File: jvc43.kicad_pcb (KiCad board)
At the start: 6 copper layers, 101.6 x 50.8 mm, 137 parts, among them J201 8P8C_LED_Shielded, J301 8P8C_LED_Shielded, J401 USB_C_Receptacle_USB2.0, U201 LAN8810, U301 LAN8810, U401 LTC3622*DE, X101 25 MHz

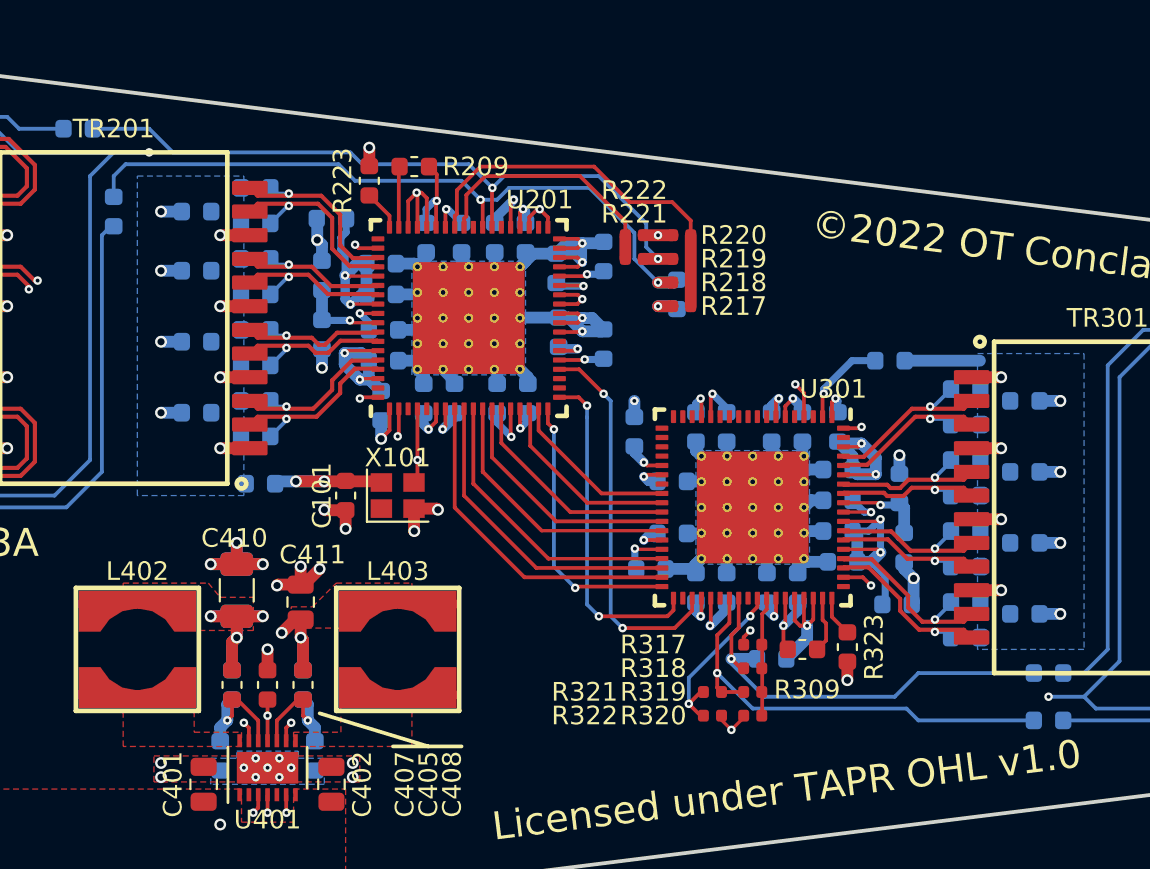
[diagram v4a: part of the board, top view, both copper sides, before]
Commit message: Added RC+D circuits for power-on reset of PHY chips.  Running out of room...
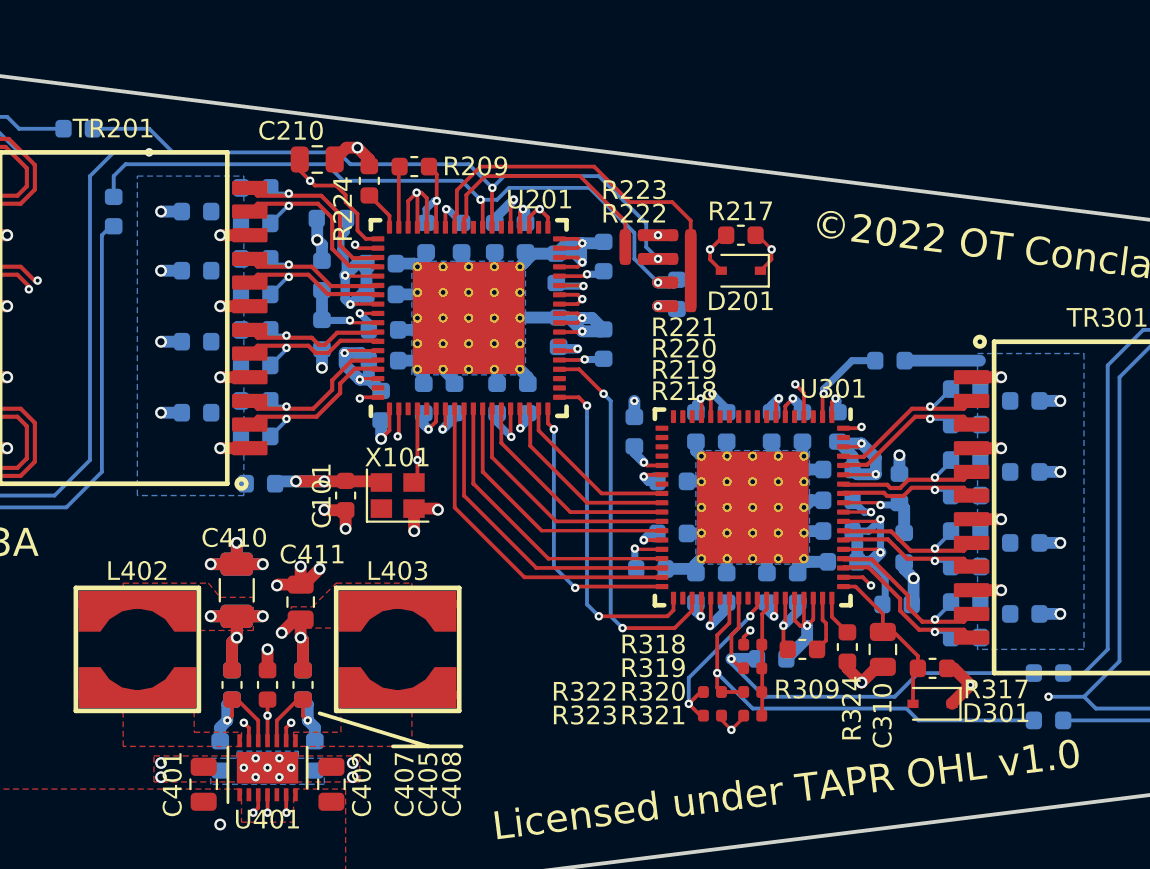
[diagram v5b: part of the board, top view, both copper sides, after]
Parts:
- added C210: 10u, Capacitor_SMD:C_0805_2012Metric, F.Cu at (60.5, 32.1)
- added C310: 10u, Capacitor_SMD:C_0805_2012Metric, F.Cu at (90.8, 58.4)
- added D201: 1N4148WS, Diode_SMD:D_SOD-323, F.Cu at (83.2, 38.1)
- added D301: 1N4148WS, Diode_SMD:D_SOD-323, F.Cu at (93.5, 61.3)
- added R217: 5k1, Resistor_SMD:R_0603_1608Metric, F.Cu at (83.2, 36.2)
- added R317: 5k1, Resistor_SMD:R_0603_1608Metric, F.Cu at (93.5, 59.4)
- renumbered C210 to C211, C211 to C212, C212 to C213, C213 to C214, C214 to C215, C215 to C216, C216 to C217, C217 to C218, C218 to C219, C219 to C220, C220 to C221, C221 to C222, C222 to C223, C223 to C224, C224 to C225, C225 to C226, C226 to C227, C227 to C228, C310 to C311, C311 to C312, C312 to C313, C313 to C314, C314 to C315, C315 to C316, C316 to C317, C317 to C318, C318 to C319, C319 to C320, C320 to C321, C321 to C322, C322 to C323, C323 to C324, C324 to C325, C325 to C326, C326 to C327, C327 to C328, R217 to R218, R218 to R219, R219 to R220, R220 to R221, R221 to R222, R222 to R223, R223 to R224, R317 to R318, R318 to R319, R319 to R320, R320 to R321, R321 to R322, R322 to R323, R323 to R324
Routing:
- net /Ethernet1/nRST: track 0.00 -> 32.8 mm, vias 0 -> 2
- net /Ethernet2/nRST: track 0.00 -> 8.78 mm
- net +2V5: track 60.5 -> 66.1 mm, vias 22 -> 24
- net GND: track 236.1 -> 239.9 mm

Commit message: Added PCB fab notes and board stackup diagram/requirements.
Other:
- board text added: "(1) PCB MATERIAL 370HR OR EQUIVALENT, THICKNESSES PER DIAGRAM"
- board text added: "(10) 100% ELECTRICAL TEST REQUIRED FOR SHORTS AND OPENS"
- board text added: "(11) IMPEDANCE: ALL 8.8 MIL WIDE / 8.1 MIL SPACE PAIRS ON LAYERS F/3 SHALL BE 100 OHMS +/- 10%. REFERENCE LAYER 2."
- board text added: "(12) VENDOR MAY ADJUST TRACE WIDTH/SPACING UP TO +/- 20% TO ACHIEVE TARGET IMPEDANCE"
- board text added: "(13) VENDOR MAY ADJUST DIELECTRIC THICKNESS TO MEET TARGET IMPEDANCE, WITHIN BOUNDS SHOWN ON STACKUP DIAGRAM"
- board text added: "(14) IMPEDANCE TESTING AND COUPON ARE NOT REQUIRED"
- board text added: "(2) APPLY GREEN LPI SOLDERMASK OVER BARE COPPER, F/B LAYERS"
- board text added: "(3) APPLY ENIG TO EXPOSED PADS, F/B LAYERS, AFTER SOLDERMASK. MIN THICKNESS 0.05 UM GOLD OVER 3 UM NICKEL."
- board text added: "(4) NOT APPLICABLE"
- board text added: "(5) SILKSCREEN WITH WHITE PERMANENT NON-CONDUCTIVE INK, F/B LAYERS"
- board text added: "(6) ADD MANUFACTURER MARKINGS SECONDARY SIDE"
- board text added: "(7) COPPER THICKNESS IN PLATED HOLES MIN AVG 25 UM, MIN THIN 20 UM"
- board text added: "(8) ALL HOLE DIAMETERS ARE FINISHED SIZES"
- board text added: "(9) FABRICATE AND INSPECT TO IPC-6012E CLASS 2"
- board text added: "0.062 INCH +/- 10%"
- board text added: "1 OZ"
- board text added: "1 OZ MIN FINISHED"
- board text added: "4-6 MILS"
- board text added: "4-6 MILS PRESSED"
- board text added: "B SECONDARY SIDE"
- board text added: "BOARD STACKUP"
- board text added: "CORE"
- board text added: "F PRIMARY SIDE"
- board text added: "L2 GROUND PLANE"
- board text added: "L3 PWR PLANE + FEW SIGNALS"
- board text added: "L4 SIGNALS + SMALL PLANES"
- board text added: "L5 PWR PLANE"
- board text added: "NOTES"
- board text added: "PREPREG"
